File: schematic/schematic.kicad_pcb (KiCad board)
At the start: 2 copper layers, 67.3 x 74.9 mm, 41 parts, among them J1 RF_In, J2 OSC3, J3 I, J4 Q, U1 CBT3253, U2 LM4562, U3 ESP32-DEVKIT, U4 Si5351A-B-GT, Y1 25MHz

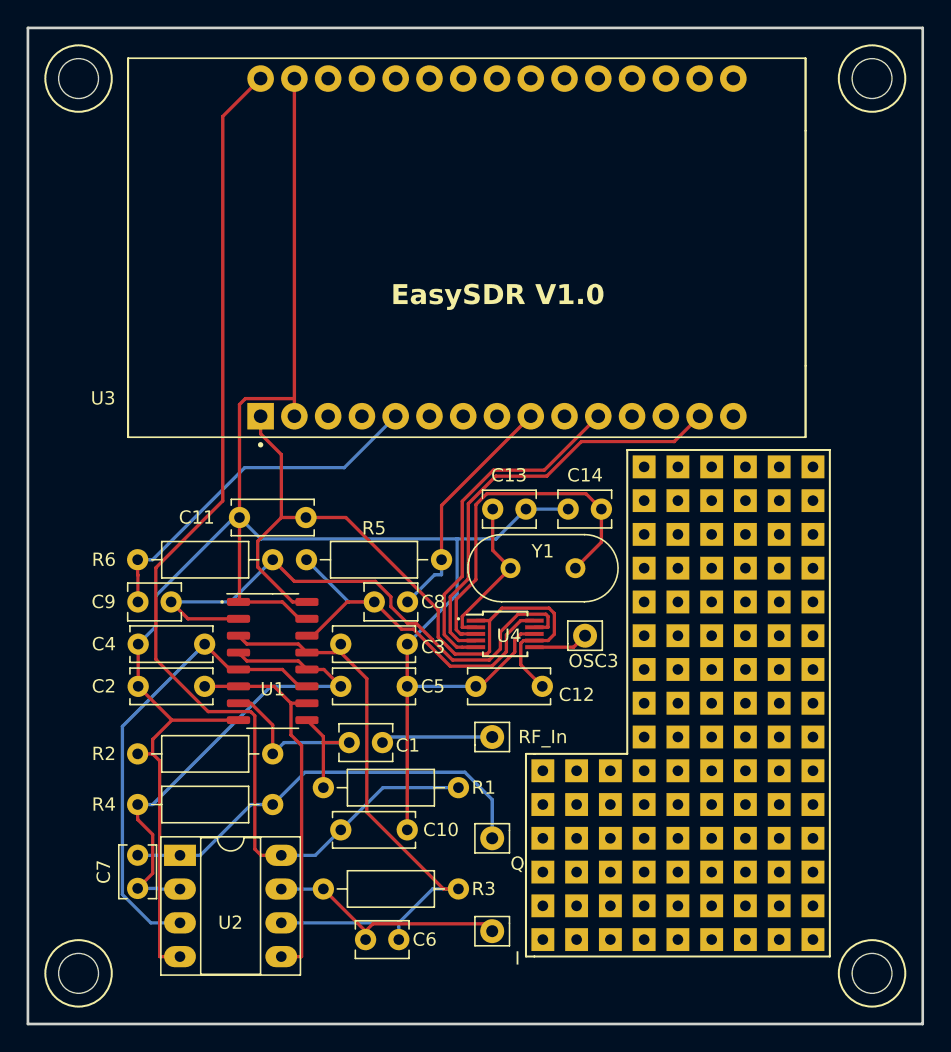
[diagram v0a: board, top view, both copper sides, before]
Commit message: Version 1.1
Supports HDSDR (Omni-rig)
Output capacitors added
Vcc pin of CBT3253 at 5V instead of 3.3V
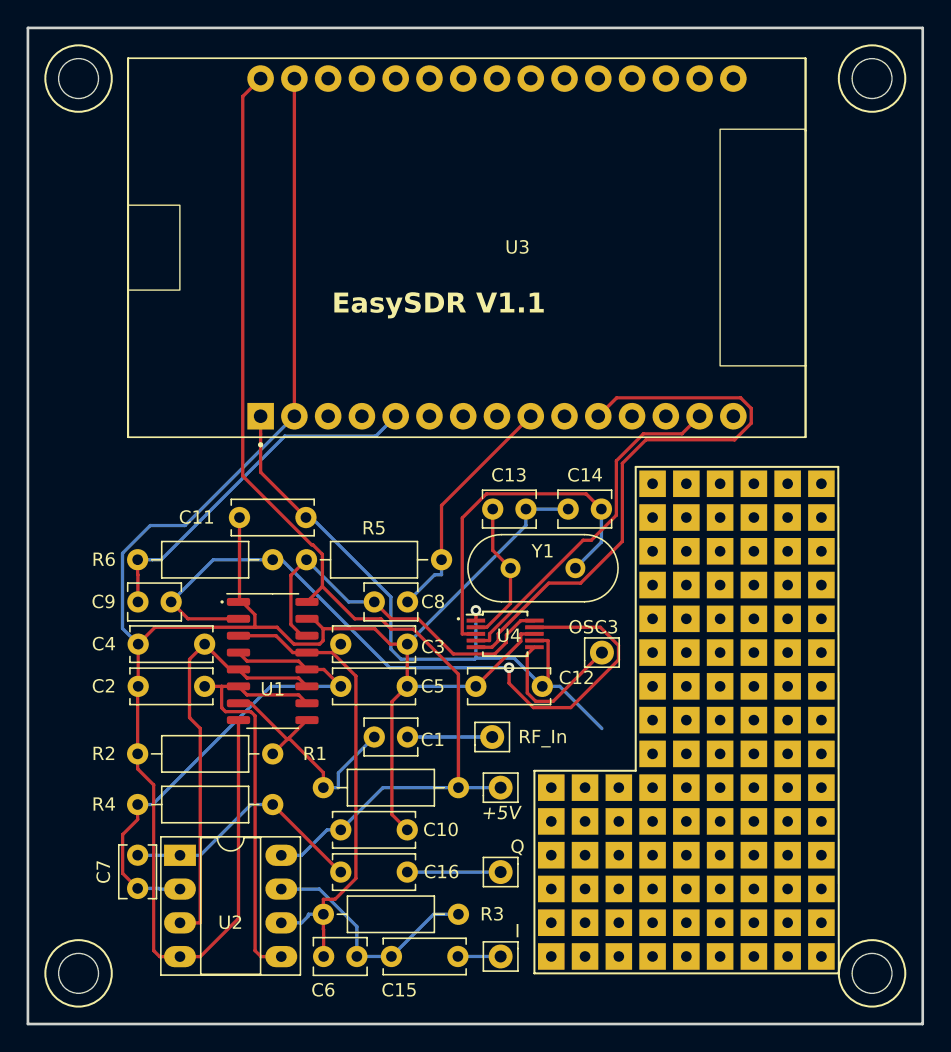
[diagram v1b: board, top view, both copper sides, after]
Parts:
- removed the REF** at (192.4, 82.5)
- removed the REF** at (184.8, 90.2)
- removed the REF** at (192.4, 105.4)
- removed the REF** at (184.8, 97.8)
- removed the REF** at (184.8, 105.4)
- removed the REF** at (177.2, 105.4)
- removed the REF** at (177.2, 97.8)
- removed the REF** at (184.8, 74.9)
- removed the REF** at (192.4, 90.2)
- removed the REF** at (192.4, 74.9)
- removed the REF** at (192.4, 97.8)
- removed the REF** at (184.8, 82.5)
- added C15: 1µ, Capacitor_THT:C_Disc_D6.0mm_W2.5mm_P5.00mm, F.Cu at (165.8, 111.8)
- added C16: 1µ, Capacitor_THT:C_Disc_D6.0mm_W2.5mm_P5.00mm, F.Cu at (162.0, 105.4)
- added J5: +5V, Connector_Pin:Pin_D0.9mm_L10.0mm_W2.4mm_FlatFork, F.Cu at (174.0, 99.1)
- added REF**: proto, parts:proto, F.Cu at (180.3, 101.6)
- added REF**: proto, parts:proto, F.Cu at (190.5, 76.2)
- added REF**: proto, parts:proto, F.Cu at (185.4, 94.0)
- added REF**: proto, parts:proto, F.Cu at (188.0, 83.8)
- added REF**: proto, parts:proto, F.Cu at (185.4, 111.8)
- added REF**: proto, parts:proto, F.Cu at (188.0, 91.4)
- added REF**: proto, parts:proto, F.Cu at (198.1, 104.1)
- added REF**: proto, parts:proto, F.Cu at (177.8, 99.1)
- added REF**: proto, parts:proto, F.Cu at (193.0, 111.8)
- added REF**: proto, parts:proto, F.Cu at (185.4, 83.8)
- added REF**: proto, parts:proto, F.Cu at (195.6, 101.6)
- added REF**: proto, parts:proto, F.Cu at (198.1, 81.3)
- added REF**: proto, parts:proto, F.Cu at (190.5, 99.1)
- added REF**: proto, parts:proto, F.Cu at (190.5, 101.6)
- added REF**: proto, parts:proto, F.Cu at (185.4, 88.9)
- added REF**: proto, parts:proto, F.Cu at (180.3, 111.8)
- added REF**: proto, parts:proto, F.Cu at (198.1, 111.8)
- added REF**: proto, parts:proto, F.Cu at (190.5, 94.0)
- added REF**: proto, parts:proto, F.Cu at (195.6, 88.9)
- added REF**: proto, parts:proto, F.Cu at (190.5, 106.7)
- added REF**: proto, parts:proto, F.Cu at (182.9, 106.7)
- added REF**: proto, parts:proto, F.Cu at (193.0, 94.0)
- added REF**: proto, parts:proto, F.Cu at (195.6, 86.4)
- added REF**: proto, parts:proto, F.Cu at (193.0, 86.4)
- added REF**: proto, parts:proto, F.Cu at (195.6, 99.1)
- added REF**: proto, parts:proto, F.Cu at (188.0, 111.8)
- added REF**: proto, parts:proto, F.Cu at (195.6, 109.2)
- added REF**: proto, parts:proto, F.Cu at (193.0, 101.6)
- added REF**: proto, parts:proto, F.Cu at (188.0, 81.3)
- added REF**: proto, parts:proto, F.Cu at (193.0, 96.5)
- added REF**: proto, parts:proto, F.Cu at (193.0, 76.2)
- added REF**: proto, parts:proto, F.Cu at (182.9, 109.2)
- added REF**: proto, parts:proto, F.Cu at (177.8, 109.2)
- added REF**: proto, parts:proto, F.Cu at (198.1, 96.5)
- added REF**: proto, parts:proto, F.Cu at (195.6, 76.2)
- added REF**: proto, parts:proto, F.Cu at (177.8, 106.7)
- added REF**: proto, parts:proto, F.Cu at (185.4, 104.1)
- added REF**: proto, parts:proto, F.Cu at (188.0, 96.5)
- added REF**: proto, parts:proto, F.Cu at (182.9, 99.1)
- added REF**: proto, parts:proto, F.Cu at (193.0, 81.3)
- added REF**: proto, parts:proto, F.Cu at (177.8, 101.6)
- added REF**: proto, parts:proto, F.Cu at (198.1, 86.4)
- added REF**: proto, parts:proto, F.Cu at (188.0, 76.2)
- added REF**: proto, parts:proto, F.Cu at (185.4, 106.7)
- added REF**: proto, parts:proto, F.Cu at (185.4, 101.6)
- added REF**: proto, parts:proto, F.Cu at (182.9, 104.1)
- added REF**: proto, parts:proto, F.Cu at (180.3, 104.1)
- added REF**: proto, parts:proto, F.Cu at (193.0, 83.8)
- added REF**: proto, parts:proto, F.Cu at (193.0, 88.9)
- added REF**: proto, parts:proto, F.Cu at (193.0, 99.1)
- added REF**: proto, parts:proto, F.Cu at (190.5, 78.7)
- added REF**: proto, parts:proto, F.Cu at (198.1, 76.2)
- added REF**: proto, parts:proto, F.Cu at (188.0, 94.0)
- added REF**: proto, parts:proto, F.Cu at (185.4, 99.1)
- added REF**: proto, parts:proto, F.Cu at (190.5, 91.4)
- added REF**: proto, parts:proto, F.Cu at (198.1, 99.1)
- added REF**: proto, parts:proto, F.Cu at (193.0, 104.1)
- added REF**: proto, parts:proto, F.Cu at (188.0, 99.1)
- added REF**: proto, parts:proto, F.Cu at (198.1, 83.8)
- added REF**: proto, parts:proto, F.Cu at (195.6, 96.5)
- added REF**: proto, parts:proto, F.Cu at (198.1, 91.4)
- added REF**: proto, parts:proto, F.Cu at (195.6, 78.7)
- added REF**: proto, parts:proto, F.Cu at (180.3, 106.7)
- added REF**: proto, parts:proto, F.Cu at (180.3, 109.2)
- added REF**: proto, parts:proto, F.Cu at (188.0, 86.4)
- added REF**: proto, parts:proto, F.Cu at (190.5, 81.3)
- added REF**: proto, parts:proto, F.Cu at (193.0, 106.7)
- added REF**: proto, parts:proto, F.Cu at (185.4, 76.2)
- added REF**: proto, parts:proto, F.Cu at (190.5, 109.2)
- added REF**: proto, parts:proto, F.Cu at (195.6, 106.7)
- added REF**: proto, parts:proto, F.Cu at (195.6, 111.8)
- added REF**: proto, parts:proto, F.Cu at (190.5, 96.5)
- added REF**: proto, parts:proto, F.Cu at (185.4, 91.4)
- added REF**: proto, parts:proto, F.Cu at (195.6, 83.8)
- added REF**: proto, parts:proto, F.Cu at (198.1, 94.0)
- added REF**: proto, parts:proto, F.Cu at (177.8, 111.8)
- added REF**: proto, parts:proto, F.Cu at (198.1, 88.9)
- added REF**: proto, parts:proto, F.Cu at (195.6, 94.0)
- added REF**: proto, parts:proto, F.Cu at (188.0, 101.6)
- added REF**: proto, parts:proto, F.Cu at (182.9, 101.6)
- added REF**: proto, parts:proto, F.Cu at (185.4, 78.7)
- added REF**: proto, parts:proto, F.Cu at (185.4, 109.2)
- added REF**: proto, parts:proto, F.Cu at (198.1, 109.2)
- added REF**: proto, parts:proto, F.Cu at (193.0, 109.2)
- added REF**: proto, parts:proto, F.Cu at (177.8, 104.1)
- added REF**: proto, parts:proto, F.Cu at (185.4, 96.5)
- added REF**: proto, parts:proto, F.Cu at (195.6, 104.1)
- added REF**: proto, parts:proto, F.Cu at (190.5, 111.8)
- added REF**: proto, parts:proto, F.Cu at (190.5, 86.4)
- added REF**: proto, parts:proto, F.Cu at (193.0, 78.7)
- added REF**: proto, parts:proto, F.Cu at (188.0, 88.9)
- added REF**: proto, parts:proto, F.Cu at (195.6, 81.3)
- added REF**: proto, parts:proto, F.Cu at (190.5, 88.9)
- added REF**: proto, parts:proto, F.Cu at (185.4, 81.3)
- added REF**: proto, parts:proto, F.Cu at (188.0, 104.1)
- added REF**: proto, parts:proto, F.Cu at (188.0, 109.2)
- added REF**: proto, parts:proto, F.Cu at (188.0, 78.7)
- added REF**: proto, parts:proto, F.Cu at (182.9, 111.8)
- added REF**: proto, parts:proto, F.Cu at (198.1, 106.7)
- added REF**: proto, parts:proto, F.Cu at (185.4, 86.4)
- added REF**: proto, parts:proto, F.Cu at (198.1, 78.7)
- added REF**: proto, parts:proto, F.Cu at (195.6, 91.4)
- added REF**: proto, parts:proto, F.Cu at (198.1, 101.6)
- added REF**: proto, parts:proto, F.Cu at (190.5, 104.1)
- added REF**: proto, parts:proto, F.Cu at (190.5, 83.8)
- added REF**: proto, parts:proto, F.Cu at (188.0, 106.7)
- added REF**: proto, parts:proto, F.Cu at (193.0, 91.4)
- added REF**: proto, parts:proto, F.Cu at (180.3, 99.1)
- R1, R2: value 1M -> 10k
- moved R3 10.3 mm to (170.8, 108.6), turned to 180 degrees
- moved C6 5.80 mm to (160.7, 111.8), turned to 0 degrees
- moved J4 2.62 mm to (174.0, 105.4)
- moved J3 2.01 mm to (174.0, 111.8)
- moved C1 1.93 mm to (164.5, 95.2)
- moved J2 1.80 mm to (181.6, 88.9)
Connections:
- C6 pad 2: Net-(J3-Pin_1) -> Net-(C15-Pad1)
- C7 pad 2: Net-(J4-Pin_1) -> Net-(C16-Pad1)
- R3 pad 1: Net-(J3-Pin_1) -> Net-(C15-Pad1)
- R4 pad 1: Net-(J4-Pin_1) -> Net-(C16-Pad1)
- U1 pad 16: +3.3V -> +5V
- U2 pad 1: Net-(J4-Pin_1) -> Net-(C16-Pad1)
- U2 pad 7: Net-(J3-Pin_1) -> Net-(C15-Pad1)
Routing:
- net Net-(J4-Pin_1): track 33.0 -> 7.03 mm
- net Net-(C16-Pad1): track 0.00 -> 19.0 mm
- net /SDA: track 26.3 -> 45.0 mm
- net Net-(C15-Pad1): track 0.00 -> 18.1 mm
- net GND: track 157.7 -> 172.9 mm
- net Net-(J3-Pin_1): track 18.3 -> 3.22 mm
- net Net-(U1-S1): track 42.9 -> 55.3 mm, vias 0 -> 1
- net Net-(U1-1B4): track 46.6 -> 37.1 mm
- net Net-(J2-Pin_1): track 4.17 -> 11.1 mm
- net +3.3V: track 55.8 -> 49.3 mm, vias 0 -> 1
- net /SCL: track 32.5 -> 26.5 mm
- net Net-(U1-1B2): track 35.6 -> 32.3 mm
- net Net-(U1-1B1): track 29.1 -> 32.4 mm
- net Net-(J1-Pin_1): track 8.43 -> 6.37 mm
- net Net-(U4-XA): track 12.0 -> 11.0 mm
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- removed copper zone on B.Cu, net GND
- removed copper zone on F.Cu, net GND
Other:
- board text added: "EasySDR V1.1"
- board text removed: "EasySDR V1.0"
